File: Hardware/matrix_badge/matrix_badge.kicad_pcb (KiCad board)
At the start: 2 copper layers, 25.4 x 38.1 mm, 35 parts, among them J1 Conn_02x03_Odd_Even, U1 ATTINY85-20SU

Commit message: Parts moved into initial spots
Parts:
- R2, R3, R4, R5, R6: moved to F.Cu
- moved R2 38.7 mm to (129.0, 108.7), turned to 90 degrees
- moved C2 37.5 mm to (136.7, 113.0), turned to 90 degrees
- moved R3 35.4 mm to (131.3, 108.7), turned to 90 degrees
- moved R1 34.9 mm to (142.7, 113.0), turned to 90 degrees
- moved C1 33.3 mm to (139.7, 113.0), turned to 90 degrees
- moved R4 32.1 mm to (133.6, 108.7), turned to 90 degrees
- moved R5 23.0 mm to (131.3, 112.8), turned to 90 degrees
- moved R6 21.7 mm to (133.6, 112.8), turned to 90 degrees
- moved J1 11.7 mm to (151.1, 111.8)
- moved S1 9.80 mm to (139.7, 110.9)
- moved D17 6.10 mm to (130.2, 105.7)
- moved D18 6.10 mm to (136.5, 105.7)
- moved D19 6.10 mm to (142.9, 105.7)
- moved D20 6.10 mm to (149.2, 105.7)
- moved D13 5.33 mm to (130.2, 100.1)
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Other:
- board size 25.4 x 38.1 mm -> 25.4 x 39.4 mm
- net class Default: clearance 0.2 -> 0.254; trace_width 0.25 -> 0.254; via_dia 0.8 -> 0.762; via_drill 0.4 -> 0.381
- rule trace_clearance: 0.2 -> 0.254
- rule trace_min: 0.2 -> 0.1524
- rule via_min_drill: 0.3 -> 0.254
- rule via_min_size: 0.4 -> 0.508

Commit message: Reconfigured footprint positions
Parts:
- moved R6 16.3 mm to (149.9, 111.8), turned to 270 degrees
- moved R5 16.0 mm to (147.3, 111.8), turned to 270 degrees
- moved R4 11.6 mm to (144.8, 111.8), turned to 270 degrees
- moved R3 11.3 mm to (142.2, 111.8), turned to 270 degrees
- moved R2 11.1 mm to (139.7, 111.8), turned to 270 degrees
- moved C2 7.12 mm to (129.5, 113.3), turned to 270 degrees
- moved S1 6.92 mm to (132.8, 111.8)
- moved J1 5.64 mm to (155.7, 115.1), turned to 0 degrees
- moved REF** 5.08 mm to (154.9, 78.7)
- moved U1 3.56 mm to (134.9, 113.0)
- moved BT1 2.54 mm to (142.2, 99.1)
- moved REF** 2.54 mm to (142.2, 81.9)
- moved D1 2.54 mm to (132.7, 83.3)
- moved D10 2.54 mm to (139.1, 94.5)
- moved D11 2.54 mm to (145.4, 94.5)
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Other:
- board size 25.4 x 39.4 mm -> 30.5 x 40.6 mm

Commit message: Layout ALMOST done. Missing 1 gnd connection.
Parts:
- moved C1 10.5 mm to (130.0, 114.6), turned to 180 degrees
- moved R1 4.64 mm to (148.6, 112.5), turned to 180 degrees
- moved C2 1.85 mm to (130.0, 111.5), turned to 180 degrees
- moved U1 0.76 mm to (135.6, 113.0)
- turned S1 to 180 degrees
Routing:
- net P3: track 0.00 -> 116.9 mm, vias 0 -> 6
- net P2: track 0.00 -> 100.8 mm, vias 0 -> 5
- net P4: track 0.00 -> 92.3 mm, vias 0 -> 5
- net P1: track 0.00 -> 87.6 mm, vias 0 -> 6
- net P5: track 0.00 -> 74.8 mm, vias 0 -> 5
- net Net-(BT1-Pad1): track 0.00 -> 54.7 mm, vias 0 -> 1
- net VDD: track 0.00 -> 43.1 mm, vias 0 -> 2
- net MISO: track 0.00 -> 33.2 mm, vias 0 -> 2
- net SCK: track 0.00 -> 27.2 mm, vias 0 -> 1
- net MOSI: track 0.00 -> 27.0 mm, vias 0 -> 1
- net ~RST: track 0.00 -> 20.8 mm
- net Net-(R6-Pad2): track 0.00 -> 13.6 mm, vias 0 -> 1
- net Net-(R5-Pad2): track 0.00 -> 10.3 mm, vias 0 -> 1
- net GND: vias 0 -> 17
- added copper zone on B.Cu, net GND
- added copper zone on F.Cu, net GND

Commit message: Finally got that last stupid #$%@# trace
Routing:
- net GND: track 0.00 -> 32.7 mm, vias 17 -> 19
- net MOSI: track 27.0 -> 25.1 mm
- net Net-(BT1-Pad1): track 54.7 -> 53.5 mm
- net SCK: track 27.2 -> 26.7 mm
- net MISO: track 33.2 -> 32.6 mm
- net Net-(R6-Pad2): track 13.6 -> 14.2 mm
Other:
- net class Default: via_dia 0.762 -> 0.6858; via_drill 0.381 -> 0.3302
- net class Power added: clearance 0.254, trace_width 0.508, via_dia 0.6858, via_drill 0.3302

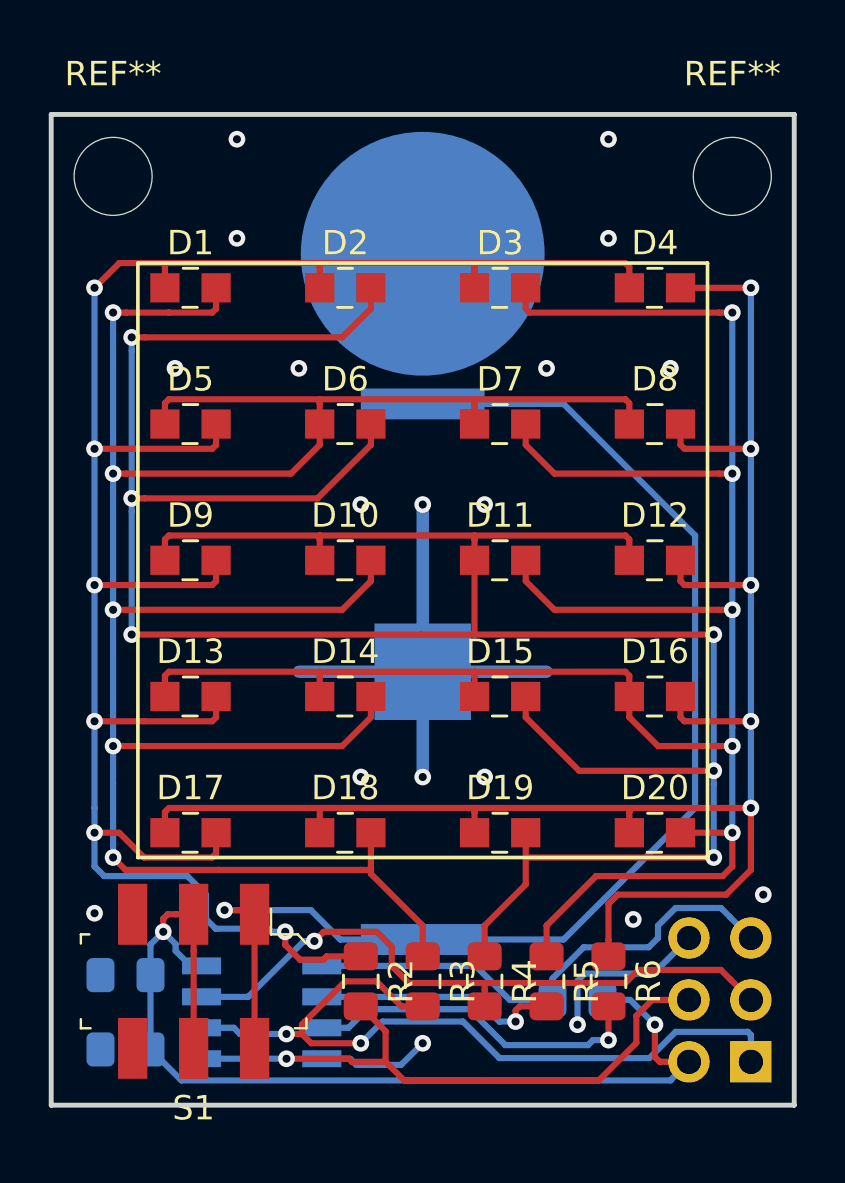
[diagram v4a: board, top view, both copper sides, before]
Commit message: Added basic silkscreen
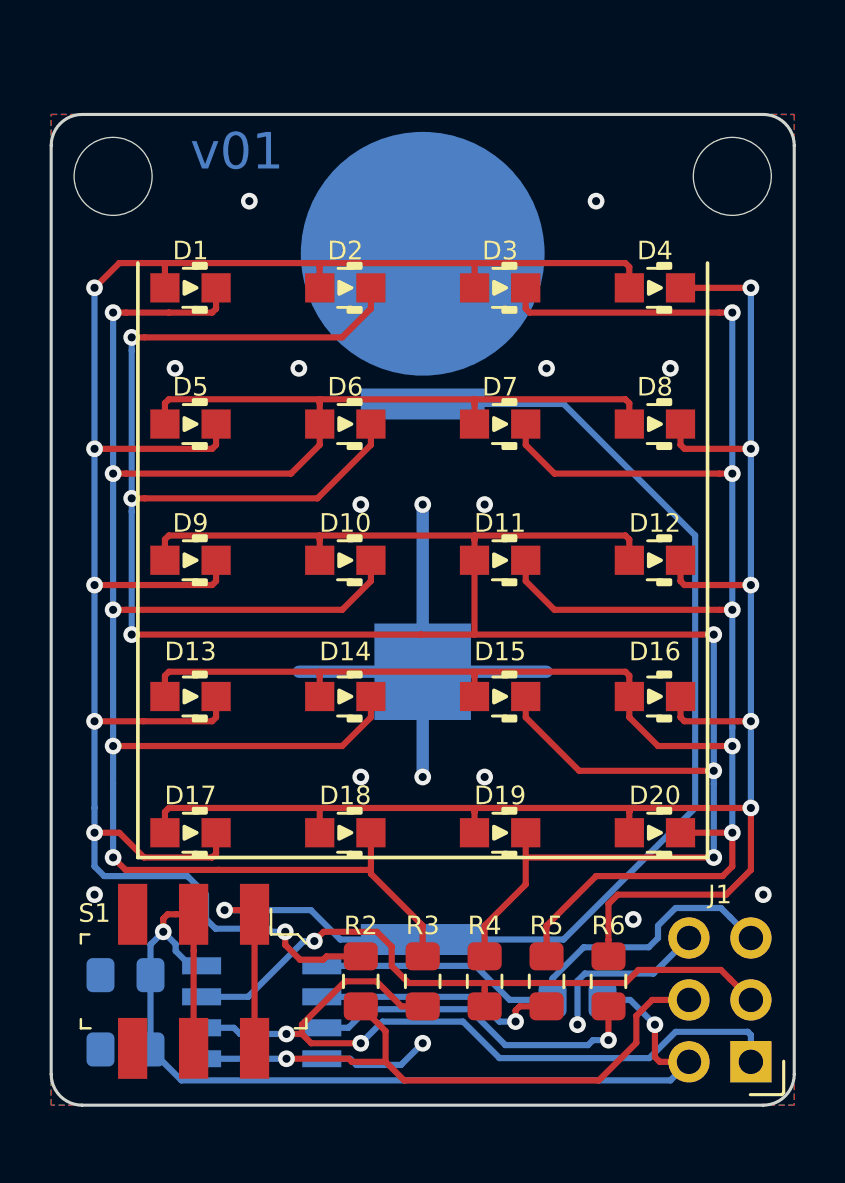
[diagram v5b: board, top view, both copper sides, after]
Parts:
- added G***: LOGO, matrix_badge:shawn_logo_silk, B.Cu at (151.1, 82.9)
- added G***: LOGO, matrix_badge:shawn_logo_copper, B.Cu at (151.2, 84.9)
- added REF**: OSHW-Symbol_6.7x6mm_SilkScreen, Symbol:OSHW-Symbol_6.7x6mm_SilkScreen, B.Cu at (133.3, 82.9)
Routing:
- net GND: vias 19 -> 17
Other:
- outline, holes or cut-outs redrawn
- board text added: "Instructions:"
- board text added: "bit.ly/2WtfLSu"
- board text added: "v01"

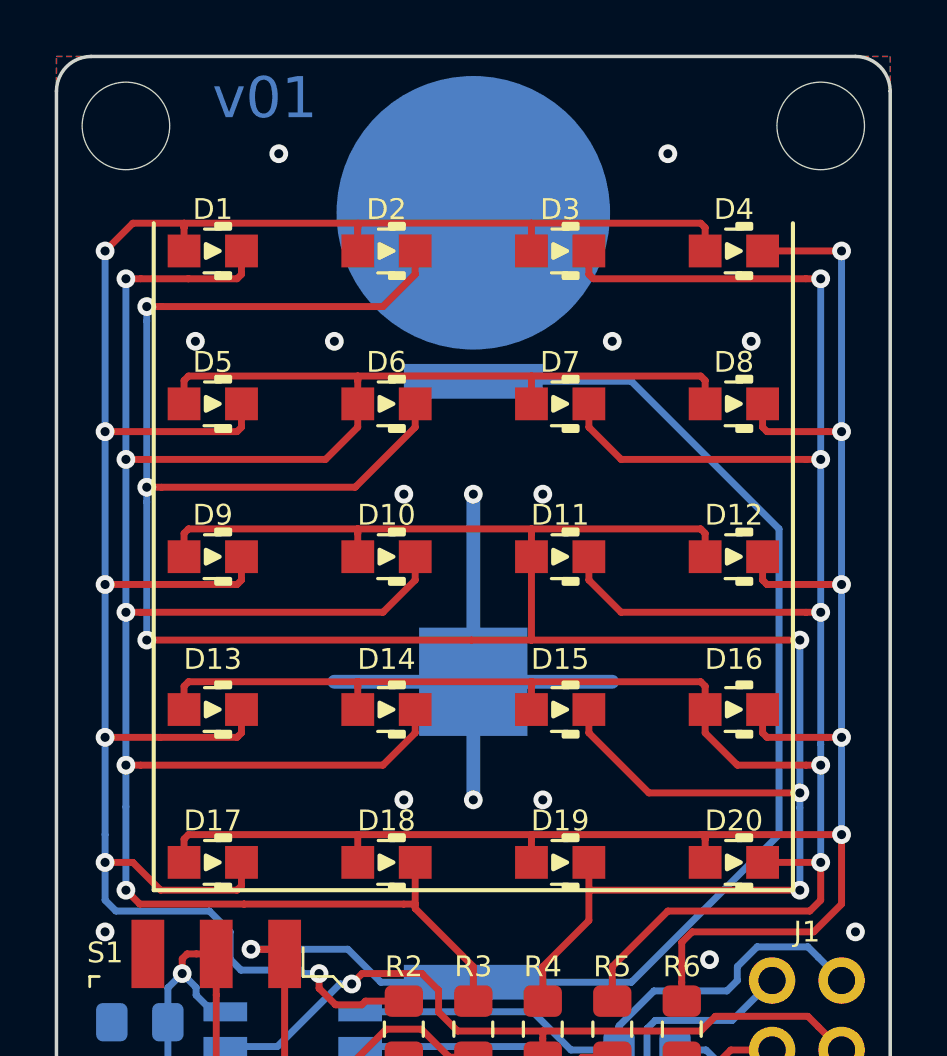
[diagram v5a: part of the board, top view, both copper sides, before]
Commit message: Added pretty silkscreen. Well, pretty by my standards.
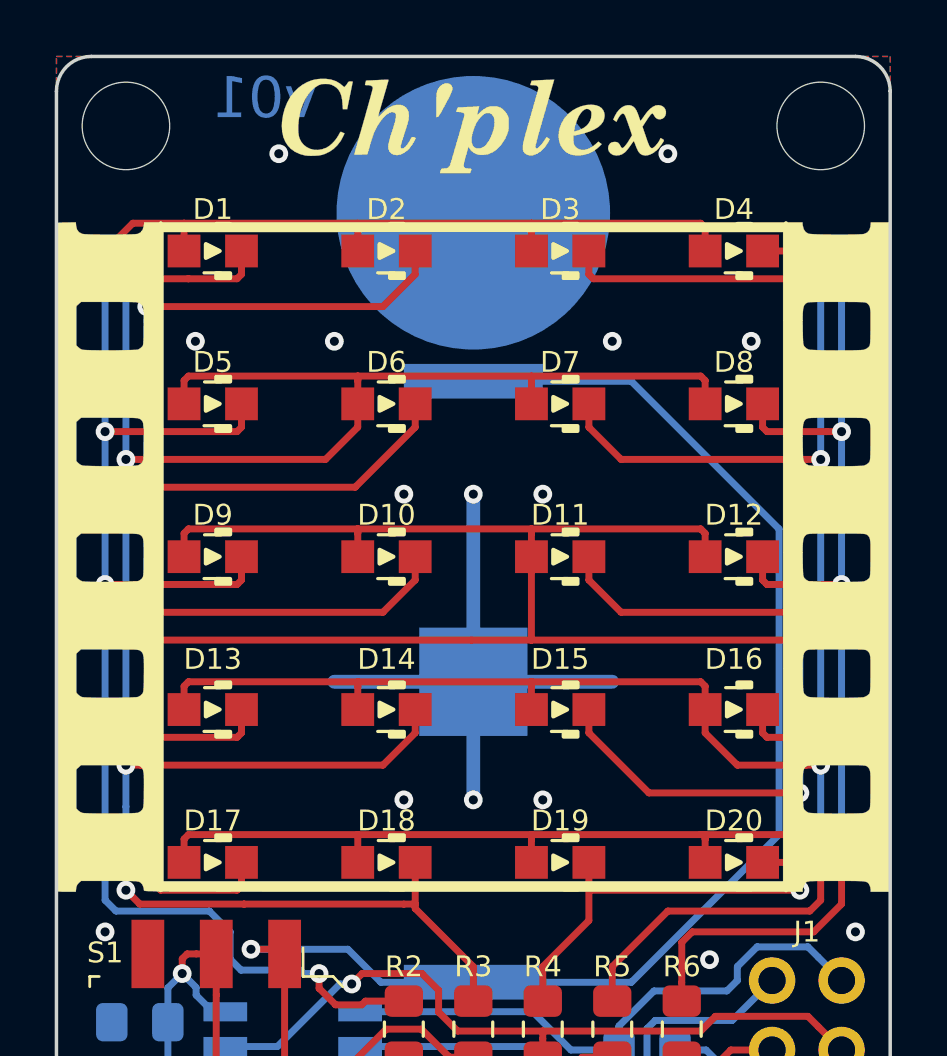
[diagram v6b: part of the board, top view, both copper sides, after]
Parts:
- added G***: LOGO, matrix_badge:chplex_logo, F.Cu at (142.2, 78.7)
- added G***: LOGO, matrix_badge:border_film, F.Cu at (142.2, 94.5)
